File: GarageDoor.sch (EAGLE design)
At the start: 35 parts, among them IC1 7805DT, J1 DCJ0202

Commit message: Add Temperature Sensor
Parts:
- removed SWITCH_CONNECT: (no value), con-lstb:MA04-1
- added JP2: RESET_SWITCH, jumper:JP1E
- added Q6: (no value), transistors:2N7000_SOT23
- added R21, R25: 100K, resistor:R-US_R0805
- added R22: 68, resistor:R-US_R0805
- added R23, R24: 100, resistor:R-US_R0805
- added R26: 10K, resistor:R-US_R0805
- added SV1: DS18B20, con-lstb:MA03-1
- added SV3: SWITCH_HEADER, con-lstb:MA04-1
- added SV6: CAMERA_HEADER, con-lstb:MA06-1
- C1: value 0.1uF -> 0.33uF
- C2: value 0.33uF -> 0.1uF
- R10: value 200 -> 100
- R11: value 68 -> 100K
- R12: value 1K -> 100
- R14: value 10K -> 1K
- R15, R20: value 10K -> 100
- R16: value 100 -> 10K
- R17, R7: value 100K -> 10K
- R18: value 1K -> 100K
- R2: value 100K -> 100
- R5: value 100 -> 100K
- R8: value 100K -> 200
- R9: value 100 -> 1K
- SV2: value (none) -> PIR_HEADER
- SV5: value (none) -> HALL_HEADER
- renumbered HALL_CONN to SV5, LED_RGB to SV4, PIEZO_HEADER to JP1, PIR_HEADER to SV2, U$1 to SC1
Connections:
- new net A1: R26.1, SC1.A1, SV1.2
- new net D6: R23.1
- new net N$19: R1.2, SV6.1
- new net N$20: R2.2, SV6.2
- new net N$21: Q6.D, SV6.5
- new net N$22: Q6.S
- new net N$23: R24.1, SV6.6
- new net N$24: Q6.G, R23.2, R25.2
- new net N$25: R25.1
- new net N$26: JP2.1, SC1.!RST
- new net RX: R2.1
- new net TX: R1.1, SC1.TX
- net +3V3: now also R26.2, R7.2, R9.2, SV1.3; no longer R18.2, R20.2
- net +5V: now also C2.1, R16.2, R17.2, SV6.4; no longer C1.1, R14.2, R15.2
- net A0: now also R7.1; no longer R20.1
- net A4: now also R10.1; no longer R3.1
- net A5: now also R15.1; no longer R4.1
- net A6: now also R20.1; no longer R5.1
- net D0: now also R3.1; no longer R1.1
- net D2: now also R9.1, SV3.1; no longer R18.1, SWITCH_CONNECT.1
- net D3: now also R13.1; no longer R12.1
- net D4: now also R14.1; no longer R13.1
- net D5: now also R4.1; no longer R16.1
- net GND: now also JP2.2, R11.1, R18.1, R21.1, R5.1, SV1.1, SV3.4, SV6.3; no longer R17.1, R2.1, R7.1, R8.1, SWITCH_CONNECT.4
- net N$1: now also R3.2, R5.2; no longer R1.2, R2.2
- net N$10: now also R12.2; no longer R9.2
- net N$11: now also R19.2; no longer R10.2
- net N$12: now also R22.2; no longer R11.2
- net N$13: now also R13.2, R17.1; no longer R12.2, R14.1
- net N$14: now also Q2.G, R4.2, R6.2; no longer Q5.G, R16.2, R17.2
- net N$15: now also R14.2, R16.1; no longer R13.2, R15.1
- net N$16: now also SV3.3; no longer SWITCH_CONNECT.3
- net N$17: now also Q2.D; no longer Q5.D
- net N$18: now also R8.1; no longer R19.1
- net N$2: now also Q4.G, R15.2; no longer Q3.G, R4.2
- net N$3: now also Q5.G, R20.2; no longer Q4.G, R5.2
- net N$4: now also Q3.G, R10.2, R11.2; no longer Q2.G, R3.2, R6.2
- net N$5: now also R18.2; no longer R7.2
- net N$6: now also R21.2; no longer R8.2
- net N$7: now also Q5.D, R22.1; no longer Q4.D, R11.1
- net N$8: now also Q4.D, R19.1; no longer Q3.D, R10.1
- net N$9: now also Q3.D, R12.1; no longer Q2.D, R9.1
- net V+: now also C1.1, R8.2; no longer C2.1, R19.2
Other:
- note added: "Camera Header Red Pin1 Brown Pin2 Purple Pin3 Gray Pin4 Red LED Pin5 Black LED Pin 6"
- moved on the sheet: C1, C2, Q2, Q3, Q4, Q5, R1, R10, R11, R12, R13, R14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

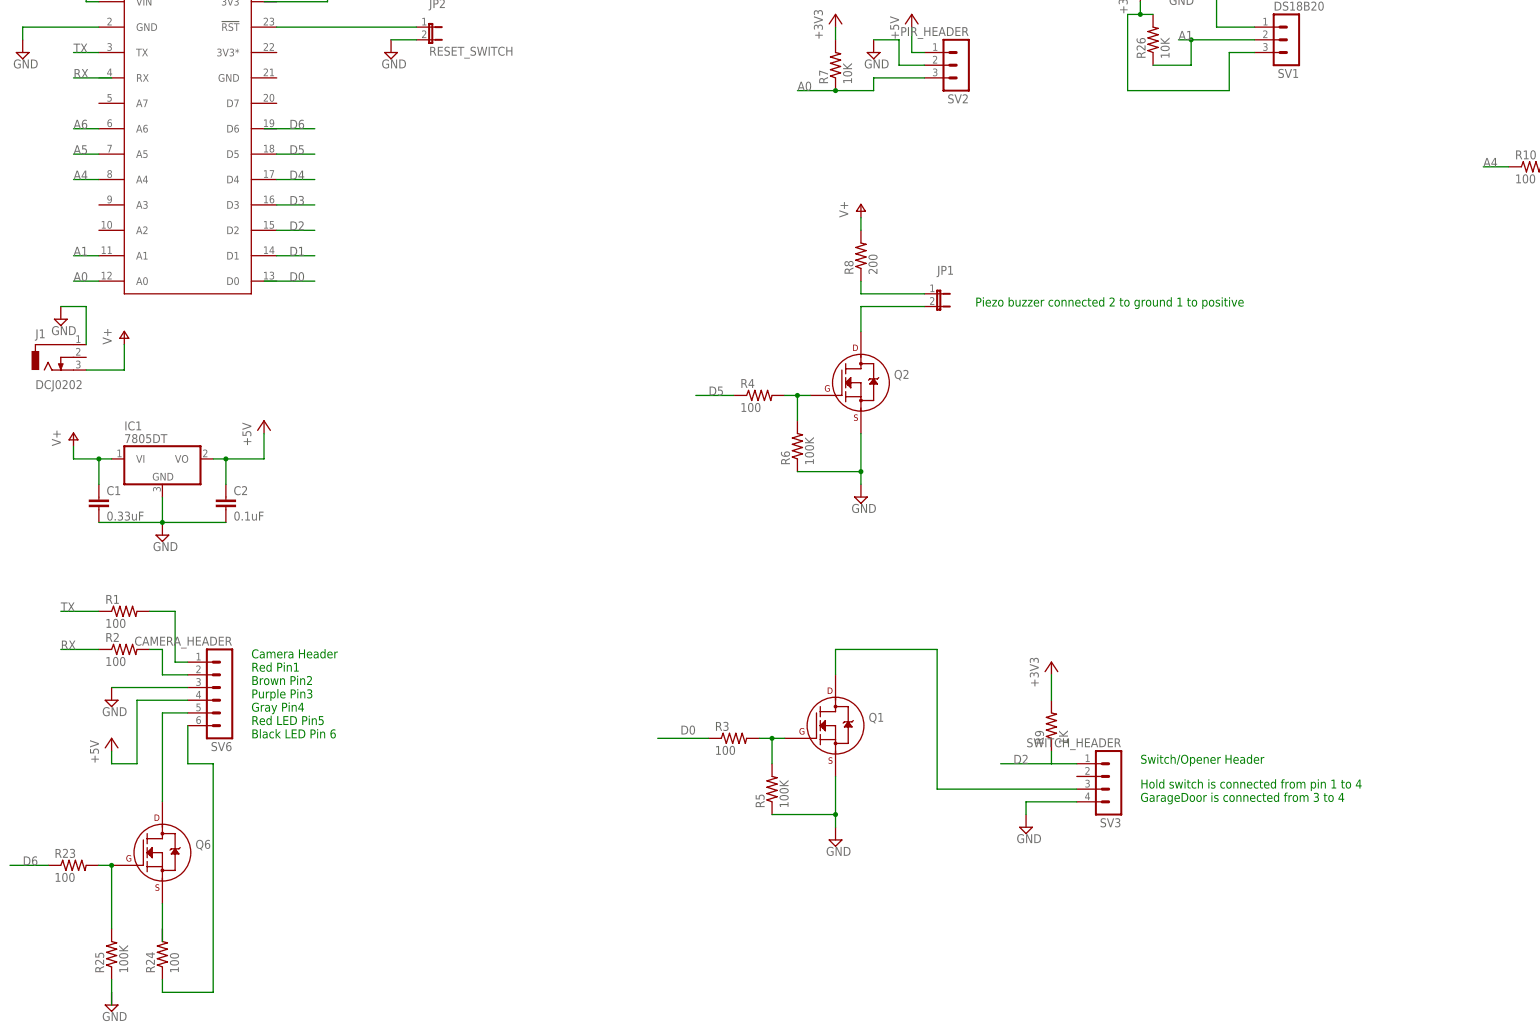
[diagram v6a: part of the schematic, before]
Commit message: Added 78LM and Hold LED
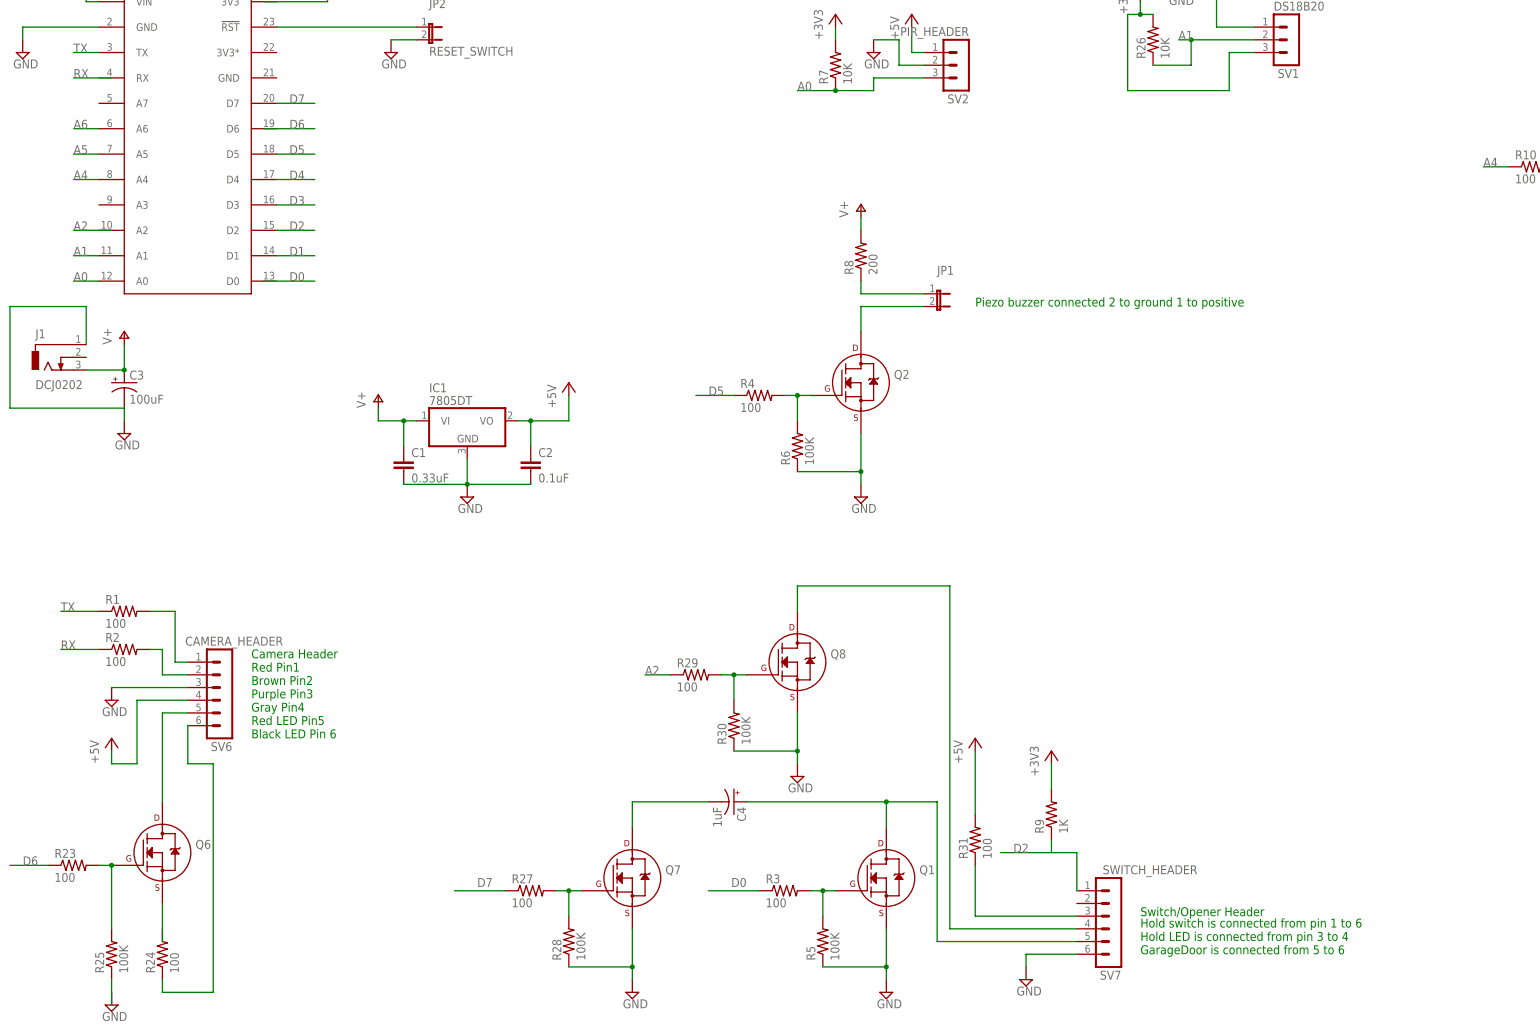
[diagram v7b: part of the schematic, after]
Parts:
- removed SV3: SWITCH_HEADER, con-lstb:MA04-1
- added C3: 100uF, rcl:CPOL-USE2,5-6E
- added C4: 1uF, rcl:CPOL-USE2,5-6E
- added Q7, Q8: (no value), transistors:2N7000_SOT23
- added R27, R29, R31: 100, resistor:R-US_R0805
- added R28, R30: 100K, resistor:R-US_R0805
- added SV7: SWITCH_HEADER, con-lstb:MA06-1
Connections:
- new net A2: R29.1
- new net D7: R27.1, SC1.D7
- new net N$27: Q7.G, R27.2, R28.2
- new net N$28: Q8.G, R29.2, R30.2
- new net N$29: C4.-, Q7.D
- new net N$30: Q8.D, SV7.4
- new net N$31: R31.1, SV7.3
- net +5V: now also R31.2
- net D2: now also SV7.1; no longer SV3.1
- net GND: now also C3.-, Q7.S, Q8.S, R28.1, R30.1, SV7.6; no longer SV3.4
- net N$16: now also C4.+, SV7.5; no longer SV3.3
- net V+: now also C3.+
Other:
- note added: "Hold switch is connected from pin 1 to 6 Hold LED is connected from pin 3 to 4 GarageDoor is connected from 5 to 6"
- note removed: "Hold switch is connected from pin 1 to 4 GarageDoor is connected from 3 to 4"
- moved on the sheet: C1, C2, IC1, Q1, R3, R5, R9

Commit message: Created PCB
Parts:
- removed C1: 0.33uF, rcl:C-EUC0805K
- removed C2: 0.1uF, rcl:C-EUC0805K
- removed IC1: 7805DT, linear:7805DT
- removed Q2, Q3, Q4, Q5, Q8: (no value), transistors:2N7000_SOT23
- removed R10, R15, R20, R29, R4: 100, resistor:R-US_R0805
- removed R11, R18, R21, R30, R6: 100K, resistor:R-US_R0805
- removed SV5: HALL_HEADER, con-lstb:MA04-1
- removed SV7: SWITCH_HEADER, con-lstb:MA06-1
- added H1, H2, H3: MOUNT-HOLE2.8, holes:MOUNT-HOLE2.8
- added J2, J3: RJ11-2L-B, con-tycoelectronics:RJ11-2L-B
- R12: value 100 -> 76
- R19: value 200 -> 68
- R22: value 68 -> 120
- R8: value 200 -> 100
- SV4: value (none) -> RGB_LED
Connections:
- removed net D0: R3.1
- removed net N$14: Q2.G, R4.2, R6.2
- removed net N$17: JP1.2, Q2.D
- removed net N$2 (its old number): Q4.G, R15.2
- removed net N$25: R25.1
- removed net N$27: Q7.G, R27.2, R28.2
- removed net N$28: Q8.G, R29.2, R30.2
- removed net N$3 (its old number): Q5.G, R20.2
- removed net N$30: Q8.D, SV7.4
- removed net N$4 (its old number): Q3.G, R10.2, R11.2
- removed net N$6: R21.2
- removed net N$7: Q5.D, R22.1
- removed net N$8: Q4.D, R19.1
- removed net N$9: Q3.D, R12.1
- removed net V+: C1.1, C3.+, IC1.VI, J1.3, R8.2
- net +3V3: now also R31.1, R7.1, R8.1, SC1.3V3, SV4.2; no longer R7.2
- net +5V: now also C3.+, J1.3, J3.2, R17.1; no longer C2.1, IC1.VO, R17.2, R31.2, SV4.2, SV5.1
- net A0: now also R7.2; no longer R7.1
- net A2: now also R23.1, SC1.A2; no longer R29.1
- net A4: now also R12.1; no longer R10.1
- net A5: now also R19.1; no longer R15.1
- net A6: now also R22.1; no longer R20.1
- net D1: now also J2.1, R9.1
- net D2: now also J2.4; no longer R9.1, SV7.1
- net D5: now also JP1.2; no longer R4.1
- net D6: now also R3.2, SC1.D6; no longer R23.1
- net D7: now also R27.2; no longer R27.1
- net GND: now also J2.6, J3.5, R25.1, R28.2, R5.2, SC1.GND@21; no longer C1.2, C2.2, IC1.GND, Q2.S, Q3.S, Q4.S, Q5.S, Q8.S, R11.1, R18.1, R21.1, R28.1, R30.1, R5.1, R6.1, SV5.4, SV7.6
- net N$1: now also R3.1, R5.1; no longer R3.2, R5.2
- net N$13: now also J3.3, R17.2; no longer R17.1, SV5.2
- net N$15: now also J3.4; no longer SV5.3
- net N$16: now also J2.5; no longer SV7.5
- net N$18: now also R8.2; no longer R8.1
- net N$22: now also R24.2
- net N$31: now also J2.3, R31.2; no longer R31.1, SV7.3
- net N$5: now also Q7.G, R27.1, R28.1; no longer R18.2
- net RX: now also SC1.RX
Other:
- note added: "RGB Led Connection"
- note removed: "RGB Led Subsystem"
- moved on the sheet: C3, C4, J1, JP1, Q1, Q6, Q7, R1, R12, R13, R14, R16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
